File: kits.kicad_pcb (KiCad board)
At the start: 2 copper layers, 40 x 40 mm, 57 parts, among them J1 10118192-0002LF, J2 S2B-PH-SM4-TB(LF)(SN), Q1 BSS138, Q2 BSS138, SW1 JS202011JCQN, SW2 TL3342F160QG, U1 MCP73811T-420I-OT, U2 TCR2EF18,LM(CT, U3 ATmega32U4RC-MU, U4 ICM-20948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

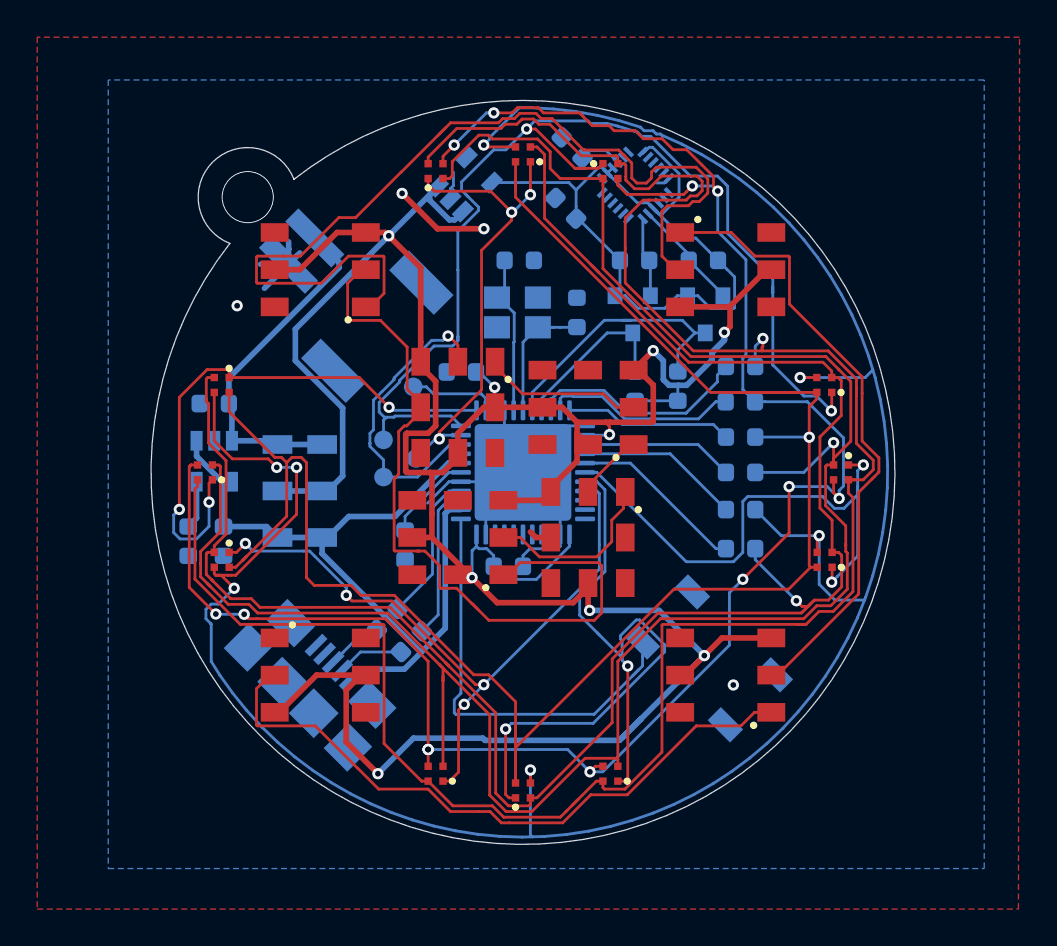
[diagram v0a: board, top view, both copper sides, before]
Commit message: Move a cap that obstructs the battery jack.
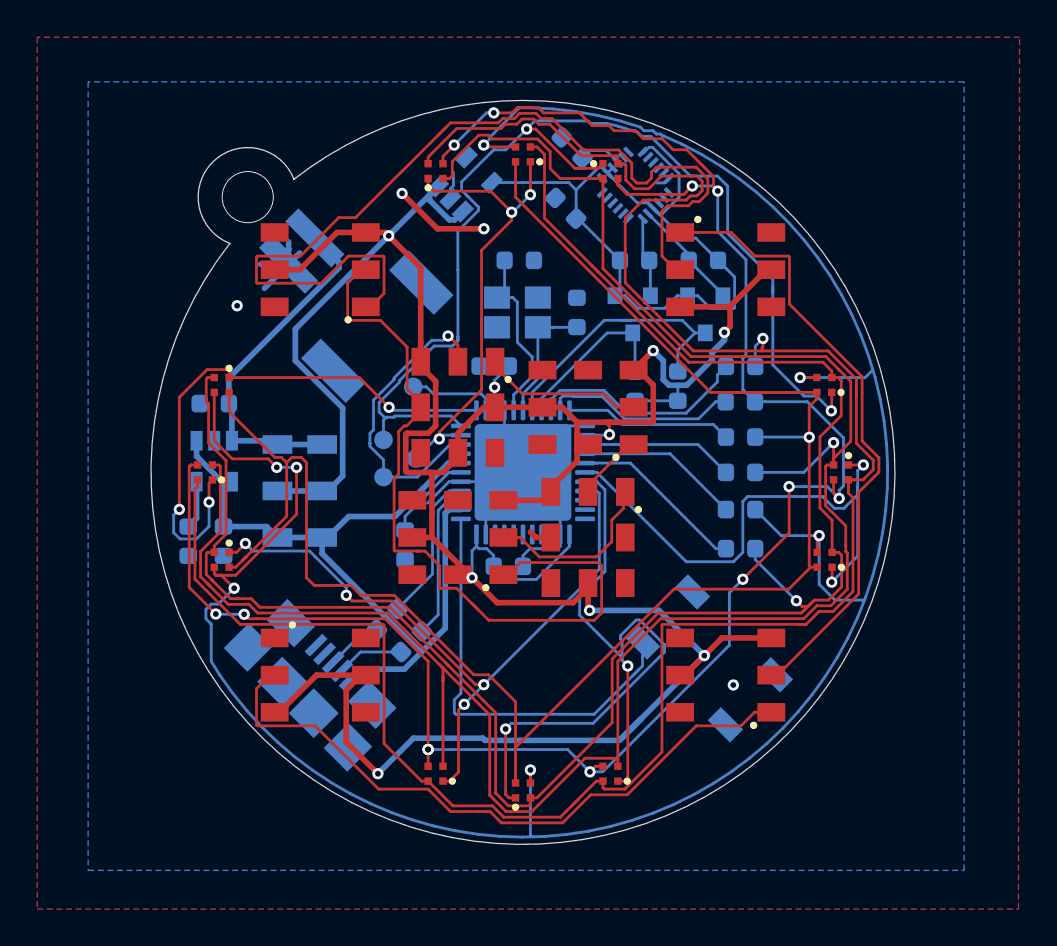
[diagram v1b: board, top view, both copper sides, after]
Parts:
- moved C7 1.79 mm to (-1.55, -5.71)
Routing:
- net Net-(C4-Pad1): track 8.69 -> 10.0 mm
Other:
- board text added: "BAT"
- board text added: "USB"
- board text removed: "Off"
- board text removed: "On"
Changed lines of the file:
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@@
-(kicad_pcb (version 20171130) (host pcbnew 5.1.2+dfsg1-1)
+(kicad_pcb (version 20171130) (host pcbnew 5.1.5-52549c5~84~ubuntu18.04.1)
   (general
     (thickness 1.6)
     (drawings 25)
-    (tracks 1198)
+    (tracks 1202)
     (zones 0)
     (modules 57)
@@
   )
   (module Capacitor_SMD:C_0603_1608Metric (layer B.Cu)
-    (at -3.3125 -5.4 180)
+    (at -1.5495 -5.715 180)
     (descr "Capacitor SMD 0603 (1608 Metric), square (rectangular) end terminal, IPC_7351 nominal, (Body size source: http://www.tortai-tech.com/upload/download/2011102023233369053.pdf), generated with kicad-footprint-generator")
     (tags capacitor)
@@
     (effects (font (size 1 1) (thickness 0.15)) (justify mirror))
   )
-  (gr_text Off (at -9.3 4.2 270) (layer B.SilkS)
+  (gr_text USB (at -9.3 4.2 270) (layer B.SilkS)
     (effects (font (size 1 1) (thickness 0.15)) (justify mirror))
   )
-  (gr_text On (at -9.3 -2.6 270) (layer B.SilkS)
+  (gr_text BAT (at -9.3 -2 270) (layer B.SilkS)
     (effects (font (size 1 1) (thickness 0.15)) (justify mirror))
   )
@@
   (segment (start -1.525 -3.3625) (end -1.5 -3.3375) (width 0.1525) (layer B.Cu) (net 20))
   (segment (start -1.525 -4.575) (end -1.525 -3.3625) (width 0.1525) (layer B.Cu) (net 20))
-  (segment (start -2.35 -5.4) (end -1.525 -4.575) (width 0.1525) (layer B.Cu) (net 20))
-  (segment (start -2.525 -5.4) (end -2.35 -5.4) (width 0.1525) (layer B.Cu) (net 20))
   (via (at 4.65 -2.03345) (size 0.6096) (drill 0.3048) (layers F.Cu B.Cu) (net 20))
   (segment (start 3.988802 -2) (end 4.61655 -2) (width 0.1525) (layer B.Cu) (net 20))
@@
   (segment (start -3.342 5.658) (end -3.5 5.5) (width 0.304) (layer F.Cu) (net 20))
   (segment (start -2.738 5.658) (end -3.342 5.658) (width 0.304) (layer F.Cu) (net 20))
+  (segment (start -1.525 -4.952) (end -0.762 -5.715) (width 0.1525) (layer B.Cu) (net 20))
+  (segment (start -1.525 -4.575) (end -1.525 -4.952) (width 0.1525) (layer B.Cu) (net 20))
   (segment (start -13.7875 2.9125) (end -13.2 3.5) (width 0.304) (layer B.Cu) (net 21))
   (segment (start -16.1 2.9125) (end -13.7875 2.9125) (width 0.304) (layer B.Cu) (net 21))
@@
   (segment (start 0.8 -7.8) (end 2 -7.8) (width 0.1525) (layer B.Cu) (net 23))
   (segment (start 2 -7.8) (end 2.8875 -7.8) (width 0.1525) (layer B.Cu) (net 23))
-  (segment (start 0 -7) (end 0.8 -7.8) (width 0.1525) (layer B.Cu) (net 23))
-  (segment (start 0 -3.3375) (end 0 -7) (width 0.1525) (layer B.Cu) (net 23))
+  (segment (start 0.8 -5.03597) (end 0.8 -7.8) (width 0.1525) (layer B.Cu) (net 23))
+  (segment (start 0 -3.3375) (end 0 -4.23597) (width 0.1525) (layer B.Cu) (net 23))
+  (segment (start 0 -4.23597) (end 0.8 -5.03597) (width 0.1525) (layer B.Cu) (net 23))
   (segment (start -0.9875 -9.8125) (end -1.4 -9.4) (width 0.1525) (layer B.Cu) (net 24))
   (segment (start -0.9875 -11.4) (end -0.9875 -9.8125) (width 0.1525) (layer B.Cu) (net 24))
   (segment (start -1.3 -9.4) (end -1.4 -9.4) (width 0.1525) (layer B.Cu) (net 24))
-  (segment (start -0.471349 -7.017079) (end -0.471349 -8.571349) (width 0.1525) (layer B.Cu) (net 24))
-  (segment (start -0.471349 -8.571349) (end -1.3 -9.4) (width 0.1525) (layer B.Cu) (net 24))
-  (segment (start -0.5 -6.988428) (end -0.471349 -7.017079) (width 0.1525) (layer B.Cu) (net 24))
-  (segment (start -0.5 -3.3375) (end -0.5 -6.988428) (width 0.1525) (layer B.Cu) (net 24))
+  (segment (start -0.5475 -9.4) (end -1.4 -9.4) (width 0.1525) (layer B.Cu) (net 24))
+  (segment (start -0.5 -4.167176) (end 0.49509 -5.162266) (width 0.1525) (layer B.Cu) (net 24))
+  (segment (start 0.49509 -5.162266) (end 0.49509 -6.20491) (width 0.1525) (layer B.Cu) (net 24))
+  (segment (start -0.5 -3.3375) (end -0.5 -4.167176) (width 0.1525) (layer B.Cu) (net 24))
+  (segment (start 0.49509 -6.20491) (end -0.3 -7) (width 0.1525) (layer B.Cu) (net 24))
+  (segment (start -0.3 -9.1525) (end -0.5475 -9.4) (width 0.1525) (layer B.Cu) (net 24))
+  (segment (start -0.3 -7) (end -0.3 -9.1525) (width 0.1525) (layer B.Cu) (net 24))
   (segment (start -3.975 0) (end -3.3375 0) (width 0.1525) (layer B.Cu) (net 25))
   (segment (start -6.34 2.365) (end -3.975 0) (width 0.1525) (layer B.Cu) (net 25))
@@
     (polygon
       (pts
-        (xy 24.8 -21.1) (xy -22.3 -21.1) (xy -22.3 21.3) (xy 24.8 21.3)
+        (xy 23.7184 -21) (xy -23.3816 -21) (xy -23.3816 21.4) (xy 23.7184 21.4)
       )
     )
